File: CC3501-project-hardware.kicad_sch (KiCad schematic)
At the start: 14 parts, among them J1 USB_C_Receptacle_USB2.0_16P, U1 RP2040, U2 AMS1117-3.3, U3 CR2013-MI2120, U4 DS18B20, U5 DS18B20, U6 DS18B20, U7 HX711

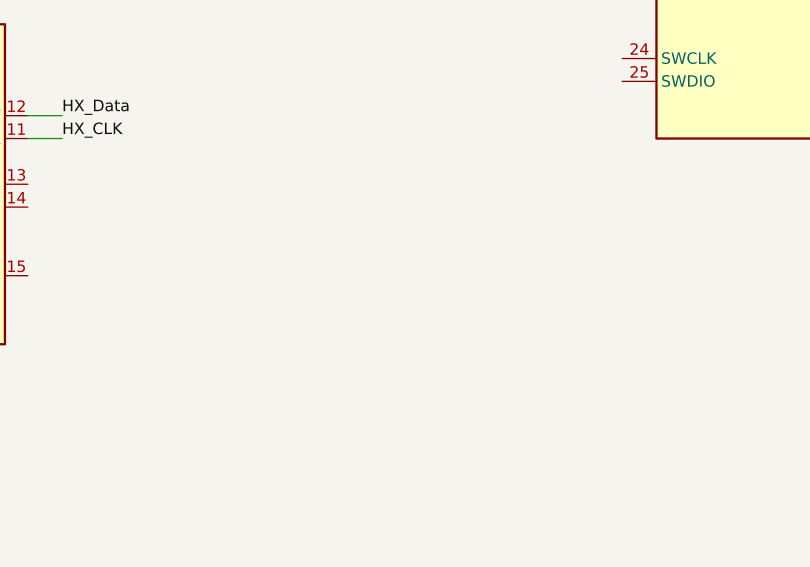
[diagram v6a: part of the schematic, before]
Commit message: Added lcsc lib and changed gitignore
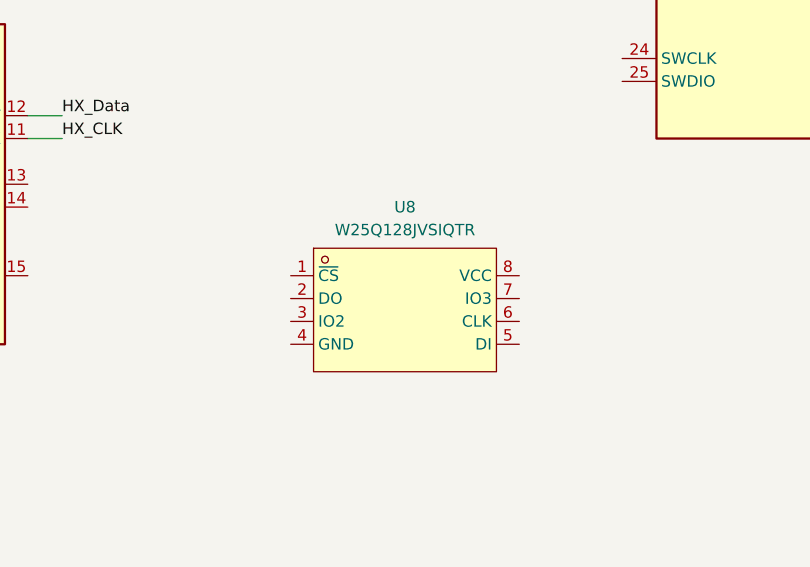
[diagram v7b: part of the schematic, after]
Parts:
- added U8: W25Q128JVSIQTR, lcsc:SOIC-8_L5.3-W5.3-P1.27-LS8.0-BL, symbol lcsc:W25Q128JVSIQTR
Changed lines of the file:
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@@
+	)
+	(symbol
+		(lib_id "lcsc:W25Q128JVSIQTR")
+		(at 171.45 129.54 0)
+		(unit 1)
+		(body_style 1)
+		(exclude_from_sim no)
+		(in_bom yes)
+		(on_board yes)
+		(in_pos_files yes)
+		(dnp no)
+		(fields_autoplaced yes)
+		(property "Reference" "U8"
+			(at 171.45 118.11 0)
+			(show_name no)
+			(do_not_autoplace no)
+			(effects
+				(font
+					(size 1.27 1.27)
+				)
+			)
+		)
+		(property "Value" "W25Q128JVSIQTR"
+			(at 171.45 120.65 0)
+			(show_name no)
+			(do_not_autoplace no)
+			(effects
+				(font
+					(size 1.27 1.27)
+				)
+			)
+		)
+		(property "Footprint" "lcsc:SOIC-8_L5.3-W5.3-P1.27-LS8.0-BL"
+			(at 171.45 140.97 0)
+			(hide yes)
+			(show_name no)
+			(do_not_autoplace no)
+			(effects
+				(font
+					(size 1.27 1.27)
+				)
+			)
+		)
+		(property "Datasheet" "https://lcsc.com/product-detail/FLASH_W25Q128JVSIQTR_C97521.html"
+			(at 171.45 143.51 0)
+			(hide yes)
+			(show_name no)
+			(do_not_autoplace no)
+			(effects
+				(font
+					(size 1.27 1.27)
+				)
+			)
+		)
+		(property "Description" ""
+			(at 171.45 129.54 0)
+			(hide yes)
+			(show_name no)
+			(do_not_autoplace no)
+			(effects
+				(font
+					(size 1.27 1.27)
+				)
+			)
+		)
+		(property "Manufacturer" "Winbond(华邦)"
+			(at 171.45 146.05 0)
+			(hide yes)
+			(show_name no)
+			(do_not_autoplace no)
+			(effects
+				(font
+					(size 1.27 1.27)
+				)
+			)
+		)
+		(property "MPN" "W25Q128JVSIQ"
+			(at 171.45 148.59 0)
+			(hide yes)
+			(show_name no)
+			(do_not_autoplace no)
+			(effects
+				(font
+					(size 1.27 1.27)
+				)
+			)
+		)
+		(property "LCSC Part" "C97521"
+			(at 171.45 151.13 0)
+			(hide yes)
+			(show_name no)
+			(do_not_autoplace no)
+			(effects
+				(font
+					(size 1.27 1.27)
+				)
+			)
+		)
+		(pin "1"
+		)
+		(pin "8"
+		)
+		(pin "7"
+		)
+		(pin "6"
+		)
+		(pin "5"
+		)
+		(pin "4"
+		)
+		(pin "3"
+		)
+		(pin "2"
+		)
+		(instances
+			(project "CC3501-project-hardware"
+				(path "/4a2d49bb-8ba4-4c60-a8f0-05b8d2544445"
+					(reference "U8")
+					(unit 1)
+				)
+			)
+		)
 	)
 	(symbol

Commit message: Flash added to sch
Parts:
- added C3: 100nF, symbol Device:C
- added J2: Conn_01x02, symbol Connector_Generic:Conn_01x02
- added R5: 10k, symbol Device:R
- added R6: 1k, symbol Device:R
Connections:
- net +3.3V: now also U8.8 (VCC), C3.1, R5.1
- net GND: now also U8.4 (GND), C3.2, J2.1 (Pin_1)
- net QSPI_SD3: now reaches U1.51 (QSPI_SD3)
- net QSPI_SD3: now also U8.7 (IO3)
- net QSPI_SCLK: now reaches U1.52 (QSPI_SCLK)
- net QSPI_SCLK: now also U8.6 (CLK)
- net QSPI_SD0: now reaches U1.53 (QSPI_SD0)
- net QSPI_SD0: now also U8.5 (DI)
- net QSPI_SD2: now reaches U1.54 (QSPI_SD2)
- net QSPI_SD2: now also U8.3 (IO2)
- net QSPI_SD1: now reaches U1.55 (QSPI_SD1)
- net QSPI_SD1: now also U8.2 (DO)
- net QSPI_SS: now reaches U1.56 (~{QSPI_SS})
- net QSPI_SS: now also U8.1 (~{CS}), R5.2, R6.2
- new net: J2.2 (Pin_2), R6.1
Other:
- note added: "Not sure if this is required. we can optionally have a bootsel bridge here. bridging QSPI_SS to GND -alister"
- note added: "all QSPI_ connections must be very short direct connections"
- moved on the sheet: C1, C2, R1, R2, R3, R4, U1, U2, U7, U8
